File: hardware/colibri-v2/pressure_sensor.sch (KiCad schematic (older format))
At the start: 6 parts

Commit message: Annotated Components
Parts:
- gave numbers to parts that had none: 6
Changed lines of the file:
@@
 $EndDescr
 $Comp
-L BMP180 U?
+L BMP180 U6
 U 1 1 558FDE4B
 P 5950 3650
-F 0 "U?" H 6300 3950 60  0000 C CNN
+F 0 "U6" H 6300 3950 60  0000 C CNN
 F 1 "BMP180" H 5700 3350 60  0000 C CNN
 F 2 "" H 5950 3650 60  0000 C CNN
@@
 PS_I2C_SCL
 $Comp
-L R R?
+L R R44
 U 1 1 558FDE8E
 P 4600 3500
-F 0 "R?" V 4550 3650 50  0000 C CNN
+F 0 "R44" V 4550 3650 50  0000 C CNN
 F 1 "22" V 4600 3500 50  0000 C CNN
 F 2 "" V 4530 3500 30  0000 C CNN
@@
 $EndComp
 $Comp
-L R R?
+L R R45
 U 1 1 558FDECD
 P 4600 3600
-F 0 "R?" V 4550 3750 50  0000 C CNN
+F 0 "R45" V 4550 3750 50  0000 C CNN
 F 1 "22" V 4600 3600 50  0000 C CNN
 F 2 "" V 4530 3600 30  0000 C CNN
@@
 	4750 3600 5250 3600
 $Comp
-L +3V3 #PWR?
+L +3V3 #PWR57
 U 1 1 558FDF78
 P 3350 2800
-F 0 "#PWR?" H 3350 2650 50  0001 C CNN
+F 0 "#PWR57" H 3350 2650 50  0001 C CNN
 F 1 "+3V3" H 3350 2940 50  0000 C CNN
 F 2 "" H 3350 2800 60  0000 C CNN
@@
 $EndComp
 $Comp
-L +3V3 #PWR?
+L +3V3 #PWR58
 U 1 1 558FDF8F
 P 3650 2800
-F 0 "#PWR?" H 3650 2650 50  0001 C CNN
+F 0 "#PWR58" H 3650 2650 50  0001 C CNN
 F 1 "+3V3" H 3650 2940 50  0000 C CNN
 F 2 "" H 3650 2800 60  0000 C CNN
@@
 $EndComp
 $Comp
-L R R?
+L R R42
 U 1 1 558FDFA7
 P 3350 3100
-F 0 "R?" H 3250 2950 50  0000 C CNN
+F 0 "R42" H 3250 2950 50  0000 C CNN
 F 1 "2k2" V 3350 3100 50  0000 C CNN
 F 2 "" V 3280 3100 30  0000 C CNN
@@
 $EndComp
 $Comp
-L R R?
+L R R43
 U 1 1 558FE0AC
 P 3650 3100
-F 0 "R?" H 3550 2950 50  0000 C CNN
+F 0 "R43" H 3550 2950 50  0000 C CNN
 F 1 "2k2" V 3650 3100 50  0000 C CNN
 F 2 "" V 3580 3100 30  0000 C CNN
@@
 Connection ~ 7100 3500
 $Comp
-L GND #PWR?
+L GND #PWR60
 U 1 1 558FE2F6
 P 7100 4550
-F 0 "#PWR?" H 7100 4300 50  0001 C CNN
+F 0 "#PWR60" H 7100 4300 50  0001 C CNN
 F 1 "GND" H 7100 4400 50  0000 C CNN
 F 2 "" H 7100 4550 60  0000 C CNN
@@
 $EndComp
 $Comp
-L GND #PWR?
+L GND #PWR59
 U 1 1 558FE312
 P 6800 4550
-F 0 "#PWR?" H 6800 4300 50  0001 C CNN
+F 0 "#PWR59" H 6800 4300 50  0001 C CNN
 F 1 "GND" H 6800 4400 50  0000 C CNN
 F 2 "" H 6800 4550 60  0000 C CNN
@@
 	6800 3800 6800 4550
 $Comp
-L C C?
+L C C54
 U 1 1 558FE33E
 P 7100 4100
-F 0 "C?" H 7125 4200 50  0000 L CNN
+F 0 "C54" H 7125 4200 50  0000 L CNN
 F 1 "100nF" H 7125 4000 50  0000 L CNN
 F 2 "" H 7138 3950 30  0000 C CNN
@@
 	7100 2200 7100 3950
 $Comp
-L PWR_FLAG #FLG?
+L PWR_FLAG #FLG2
 U 1 1 55FF4C0A
 P 3500 1850
-F 0 "#FLG?" H 3500 1945 50  0001 C CNN
+F 0 "#FLG2" H 3500 1945 50  0001 C CNN
 F 1 "PWR_FLAG" H 3500 2030 50  0000 C CNN
 F 2 "" H 3500 1850 60  0000 C CNN

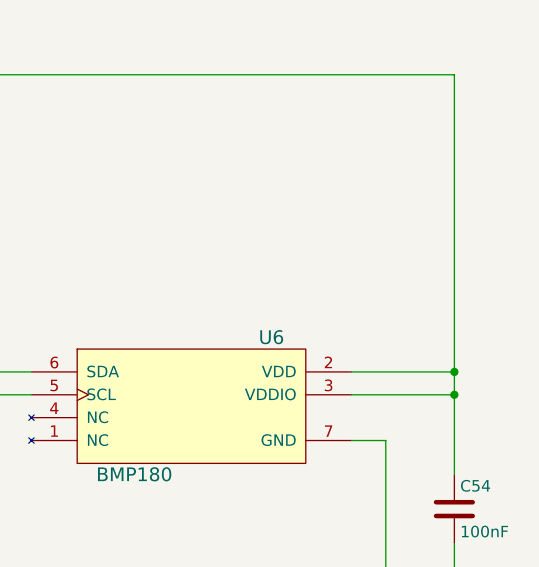
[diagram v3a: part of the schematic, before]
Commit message: Use separate VDD IO
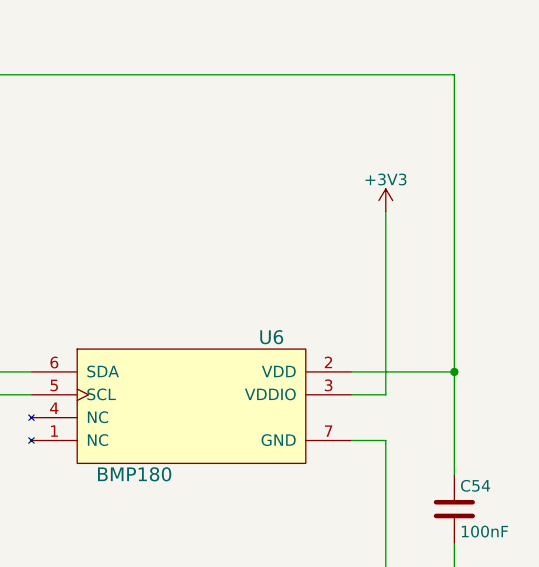
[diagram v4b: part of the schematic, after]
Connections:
- net +3V3: now also U6.3 (VDDIO)
- net V_SENS1: no longer U6.3 (VDDIO)
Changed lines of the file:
@@
 	4750 3600 5250 3600
 $Comp
-L +3V3 #PWR57
+L +3V3 #PWR058
 U 1 1 558FDF78
 P 3350 2800
-F 0 "#PWR57" H 3350 2650 50  0001 C CNN
+F 0 "#PWR058" H 3350 2650 50  0001 C CNN
 F 1 "+3V3" H 3350 2940 50  0000 C CNN
 F 2 "" H 3350 2800 60  0000 C CNN
@@
 $EndComp
 $Comp
-L +3V3 #PWR58
+L +3V3 #PWR059
 U 1 1 558FDF8F
 P 3650 2800
-F 0 "#PWR58" H 3650 2650 50  0001 C CNN
+F 0 "#PWR059" H 3650 2650 50  0001 C CNN
 F 1 "+3V3" H 3650 2940 50  0000 C CNN
 F 2 "" H 3650 2800 60  0000 C CNN
@@
 Wire Wire Line
 	7100 3500 6650 3500
-Wire Wire Line
-	7100 3600 6650 3600
 Connection ~ 7100 3500
 $Comp
-L GND #PWR60
+L GND #PWR060
 U 1 1 558FE2F6
 P 7100 4550
-F 0 "#PWR60" H 7100 4300 50  0001 C CNN
+F 0 "#PWR060" H 7100 4300 50  0001 C CNN
 F 1 "GND" H 7100 4400 50  0000 C CNN
 F 2 "" H 7100 4550 60  0000 C CNN
@@
 $EndComp
 $Comp
-L GND #PWR59
+L GND #PWR061
 U 1 1 558FE312
 P 6800 4550
-F 0 "#PWR59" H 6800 4300 50  0001 C CNN
+F 0 "#PWR061" H 6800 4300 50  0001 C CNN
 F 1 "GND" H 6800 4400 50  0000 C CNN
 F 2 "" H 6800 4550 60  0000 C CNN
@@
 	1    0    0    -1
 $EndComp
-Connection ~ 7100 3600
 Wire Wire Line
 	7100 4250 7100 4550
@@
 	7100 2200 7100 3950
 $Comp
-L PWR_FLAG #FLG2
+L PWR_FLAG #FLG062
 U 1 1 55FF4C0A
 P 3500 1850
-F 0 "#FLG2" H 3500 1945 50  0001 C CNN
+F 0 "#FLG062" H 3500 1945 50  0001 C CNN
 F 1 "PWR_FLAG" H 3500 2030 50  0000 C CNN
 F 2 "" H 3500 1850 60  0000 C CNN
@@
 	3500 1850 3500 2200
 Connection ~ 3500 2200
+$Comp
+L +3V3 #PWR?
+U 1 1 562303A9
+P 6800 2800
+F 0 "#PWR?" H 6800 2650 50  0001 C CNN
+F 1 "+3V3" H 6800 2940 50  0000 C CNN
+F 2 "" H 6800 2800 60  0000 C CNN
+F 3 "" H 6800 2800 60  0000 C CNN
+	1    6800 2800
+	1    0    0    -1
+$EndComp
+Wire Wire Line
+	6650 3600 6800 3600
+Wire Wire Line
+	6800 3600 6800 2800
 $EndSCHEMATC

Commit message: Re-annotated schematic
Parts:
- renumbered C54 to C52, R42 to R43, R43 to R44, R44 to R45, R45 to R46
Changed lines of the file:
@@
 PS_I2C_SCL
 $Comp
-L R R44
+L R R45
 U 1 1 558FDE8E
 P 4600 3500
-F 0 "R44" V 4550 3650 50  0000 C CNN
+F 0 "R45" V 4550 3650 50  0000 C CNN
 F 1 "22" V 4600 3500 50  0000 C CNN
 F 2 "" V 4530 3500 30  0000 C CNN
@@
 $EndComp
 $Comp
-L R R45
+L R R46
 U 1 1 558FDECD
 P 4600 3600
-F 0 "R45" V 4550 3750 50  0000 C CNN
+F 0 "R46" V 4550 3750 50  0000 C CNN
 F 1 "22" V 4600 3600 50  0000 C CNN
 F 2 "" V 4530 3600 30  0000 C CNN
@@
 	4750 3600 5250 3600
 $Comp
-L +3V3 #PWR058
+L +3V3 #PWR53
 U 1 1 558FDF78
 P 3350 2800
-F 0 "#PWR058" H 3350 2650 50  0001 C CNN
+F 0 "#PWR53" H 3350 2650 50  0001 C CNN
 F 1 "+3V3" H 3350 2940 50  0000 C CNN
 F 2 "" H 3350 2800 60  0000 C CNN
@@
 $EndComp
 $Comp
-L +3V3 #PWR059
+L +3V3 #PWR54
 U 1 1 558FDF8F
 P 3650 2800
-F 0 "#PWR059" H 3650 2650 50  0001 C CNN
+F 0 "#PWR54" H 3650 2650 50  0001 C CNN
 F 1 "+3V3" H 3650 2940 50  0000 C CNN
 F 2 "" H 3650 2800 60  0000 C CNN
@@
 $EndComp
 $Comp
-L R R42
+L R R43
 U 1 1 558FDFA7
 P 3350 3100
-F 0 "R42" H 3250 2950 50  0000 C CNN
+F 0 "R43" H 3250 2950 50  0000 C CNN
 F 1 "2k2" V 3350 3100 50  0000 C CNN
 F 2 "" V 3280 3100 30  0000 C CNN
@@
 $EndComp
 $Comp
-L R R43
+L R R44
 U 1 1 558FE0AC
 P 3650 3100
-F 0 "R43" H 3550 2950 50  0000 C CNN
+F 0 "R44" H 3550 2950 50  0000 C CNN
 F 1 "2k2" V 3650 3100 50  0000 C CNN
 F 2 "" V 3580 3100 30  0000 C CNN
@@
 Connection ~ 7100 3500
 $Comp
-L GND #PWR060
+L GND #PWR57
 U 1 1 558FE2F6
 P 7100 4550
-F 0 "#PWR060" H 7100 4300 50  0001 C CNN
+F 0 "#PWR57" H 7100 4300 50  0001 C CNN
 F 1 "GND" H 7100 4400 50  0000 C CNN
 F 2 "" H 7100 4550 60  0000 C CNN
@@
 $EndComp
 $Comp
-L GND #PWR061
+L GND #PWR56
 U 1 1 558FE312
 P 6800 4550
-F 0 "#PWR061" H 6800 4300 50  0001 C CNN
+F 0 "#PWR56" H 6800 4300 50  0001 C CNN
 F 1 "GND" H 6800 4400 50  0000 C CNN
 F 2 "" H 6800 4550 60  0000 C CNN
@@
 	6800 3800 6800 4550
 $Comp
-L C C54
+L C C52
 U 1 1 558FE33E
 P 7100 4100
-F 0 "C54" H 7125 4200 50  0000 L CNN
+F 0 "C52" H 7125 4200 50  0000 L CNN
 F 1 "100nF" H 7125 4000 50  0000 L CNN
 F 2 "" H 7138 3950 30  0000 C CNN
@@
 	7100 2200 7100 3950
 $Comp
-L PWR_FLAG #FLG062
+L PWR_FLAG #FLG2
 U 1 1 55FF4C0A
 P 3500 1850
-F 0 "#FLG062" H 3500 1945 50  0001 C CNN
+F 0 "#FLG2" H 3500 1945 50  0001 C CNN
 F 1 "PWR_FLAG" H 3500 2030 50  0000 C CNN
 F 2 "" H 3500 1850 60  0000 C CNN
@@
 Connection ~ 3500 2200
 $Comp
-L +3V3 #PWR?
+L +3V3 #PWR55
 U 1 1 562303A9
 P 6800 2800
-F 0 "#PWR?" H 6800 2650 50  0001 C CNN
+F 0 "#PWR55" H 6800 2650 50  0001 C CNN
 F 1 "+3V3" H 6800 2940 50  0000 C CNN
 F 2 "" H 6800 2800 60  0000 C CNN

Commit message: Associated footprints for R and some of the C
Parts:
- C52: footprint (none) -> Capacitors_SMD:C_0805
- R43, R44, R45, R46: footprint (none) -> Resistors_SMD:R_0603
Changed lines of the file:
@@
 F 0 "U6" H 6300 3950 60  0000 C CNN
 F 1 "BMP180" H 5700 3350 60  0000 C CNN
-F 2 "" H 5950 3650 60  0000 C CNN
+F 2 "" H 5950 3650 60  0001 C CNN
 F 3 "" H 5950 3650 60  0000 C CNN
 	1    5950 3650
@@
 F 0 "R45" V 4550 3650 50  0000 C CNN
 F 1 "22" V 4600 3500 50  0000 C CNN
-F 2 "" V 4530 3500 30  0000 C CNN
+F 2 "Resistors_SMD:R_0603" V 4530 3500 30  0001 C CNN
 F 3 "" H 4600 3500 30  0000 C CNN
 	1    4600 3500
@@
 F 0 "R46" V 4550 3750 50  0000 C CNN
 F 1 "22" V 4600 3600 50  0000 C CNN
-F 2 "" V 4530 3600 30  0000 C CNN
+F 2 "Resistors_SMD:R_0603" V 4530 3600 30  0001 C CNN
 F 3 "" H 4600 3600 30  0000 C CNN
 	1    4600 3600
@@
 	4750 3600 5250 3600
 $Comp
-L +3V3 #PWR53
+L +3V3 #PWR054
 U 1 1 558FDF78
 P 3350 2800
-F 0 "#PWR53" H 3350 2650 50  0001 C CNN
+F 0 "#PWR054" H 3350 2650 50  0001 C CNN
 F 1 "+3V3" H 3350 2940 50  0000 C CNN
 F 2 "" H 3350 2800 60  0000 C CNN
@@
 $EndComp
 $Comp
-L +3V3 #PWR54
+L +3V3 #PWR055
 U 1 1 558FDF8F
 P 3650 2800
-F 0 "#PWR54" H 3650 2650 50  0001 C CNN
+F 0 "#PWR055" H 3650 2650 50  0001 C CNN
 F 1 "+3V3" H 3650 2940 50  0000 C CNN
 F 2 "" H 3650 2800 60  0000 C CNN
@@
 F 0 "R43" H 3250 2950 50  0000 C CNN
 F 1 "2k2" V 3350 3100 50  0000 C CNN
-F 2 "" V 3280 3100 30  0000 C CNN
+F 2 "Resistors_SMD:R_0603" V 3280 3100 30  0001 C CNN
 F 3 "" H 3350 3100 30  0000 C CNN
 	1    3350 3100
@@
 F 0 "R44" H 3550 2950 50  0000 C CNN
 F 1 "2k2" V 3650 3100 50  0000 C CNN
-F 2 "" V 3580 3100 30  0000 C CNN
+F 2 "Resistors_SMD:R_0603" V 3580 3100 30  0001 C CNN
 F 3 "" H 3650 3100 30  0000 C CNN
 	1    3650 3100
@@
 Connection ~ 7100 3500
 $Comp
-L GND #PWR57
+L GND #PWR056
 U 1 1 558FE2F6
 P 7100 4550
-F 0 "#PWR57" H 7100 4300 50  0001 C CNN
+F 0 "#PWR056" H 7100 4300 50  0001 C CNN
 F 1 "GND" H 7100 4400 50  0000 C CNN
 F 2 "" H 7100 4550 60  0000 C CNN
@@
 $EndComp
 $Comp
-L GND #PWR56
+L GND #PWR057
 U 1 1 558FE312
 P 6800 4550
-F 0 "#PWR56" H 6800 4300 50  0001 C CNN
+F 0 "#PWR057" H 6800 4300 50  0001 C CNN
 F 1 "GND" H 6800 4400 50  0000 C CNN
 F 2 "" H 6800 4550 60  0000 C CNN
@@
 F 0 "C52" H 7125 4200 50  0000 L CNN
 F 1 "100nF" H 7125 4000 50  0000 L CNN
-F 2 "" H 7138 3950 30  0000 C CNN
+F 2 "Capacitors_SMD:C_0805" H 7138 3950 30  0001 C CNN
 F 3 "" H 7100 4100 60  0000 C CNN
 	1    7100 4100
@@
 	7100 2200 7100 3950
 $Comp
-L PWR_FLAG #FLG2
+L PWR_FLAG #FLG058
 U 1 1 55FF4C0A
 P 3500 1850
-F 0 "#FLG2" H 3500 1945 50  0001 C CNN
+F 0 "#FLG058" H 3500 1945 50  0001 C CNN
 F 1 "PWR_FLAG" H 3500 2030 50  0000 C CNN
 F 2 "" H 3500 1850 60  0000 C CNN
@@
 Connection ~ 3500 2200
 $Comp
-L +3V3 #PWR55
+L +3V3 #PWR059
 U 1 1 562303A9
 P 6800 2800
-F 0 "#PWR55" H 6800 2650 50  0001 C CNN
+F 0 "#PWR059" H 6800 2650 50  0001 C CNN
 F 1 "+3V3" H 6800 2940 50  0000 C CNN
 F 2 "" H 6800 2800 60  0000 C CNN

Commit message: Work on cortex USB connection.
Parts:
- removed C52: 100nF, Capacitors_SMD:C_0805, symbol C
- removed R43, R44: 2k2, Resistors_SMD:R_0603, symbol R
- removed R45, R46: 22, Resistors_SMD:R_0603, symbol R
- added C?: 100nF/50V, Capacitors_SMD:C_0603, symbol C_SMT
- added R? (x2): 2k2/5%, Resistors_SMD:R_0603, symbol R_SMT
- added R? (x2): 22R/5%, Resistors_SMD:R_0603, symbol R_SMT
- renumbered U6 to U?
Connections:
- net +3V3: now also R?.1, R?.1
- net GND: now also C?.2
- net PS_I2C_SCL: now also R?.2, R?.2
- net PS_I2C_SDA: now also R?.2, R?.2
- net V_SENS1: now also C?.1
- net at U?.5 (SCL): now also R?.1
- net at U?.6 (SDA): now also R?.1
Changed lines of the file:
@@
 $EndDescr
 $Comp
-L BMP180 U6
+L BMP180 U?
 U 1 1 558FDE4B
 P 5950 3650
-F 0 "U6" H 6300 3950 60  0000 C CNN
+F 0 "U?" H 6300 3950 60  0000 C CNN
 F 1 "BMP180" H 5700 3350 60  0000 C CNN
 F 2 "" H 5950 3650 60  0001 C CNN
@@
 Text HLabel 2950 3600 0    60   Input ~ 0
 PS_I2C_SCL
-$Comp
-L R R45
-U 1 1 558FDE8E
-P 4600 3500
-F 0 "R45" V 4550 3650 50  0000 C CNN
-F 1 "22" V 4600 3500 50  0000 C CNN
-F 2 "Resistors_SMD:R_0603" V 4530 3500 30  0001 C CNN
-F 3 "" H 4600 3500 30  0000 C CNN
-	1    4600 3500
-	0    1    1    0
-$EndComp
-$Comp
-L R R46
-U 1 1 558FDECD
-P 4600 3600
-F 0 "R46" V 4550 3750 50  0000 C CNN
-F 1 "22" V 4600 3600 50  0000 C CNN
-F 2 "Resistors_SMD:R_0603" V 4530 3600 30  0001 C CNN
-F 3 "" H 4600 3600 30  0000 C CNN
-	1    4600 3600
-	0    1    1    0
-$EndComp
 Wire Wire Line
 	2950 3500 4450 3500
@@
 	4750 3600 5250 3600
 $Comp
-L +3V3 #PWR054
+L +3V3 #PWR?
 U 1 1 558FDF78
 P 3350 2800
-F 0 "#PWR054" H 3350 2650 50  0001 C CNN
+F 0 "#PWR?" H 3350 2650 50  0001 C CNN
 F 1 "+3V3" H 3350 2940 50  0000 C CNN
 F 2 "" H 3350 2800 60  0000 C CNN
@@
 $EndComp
 $Comp
-L +3V3 #PWR055
+L +3V3 #PWR?
 U 1 1 558FDF8F
 P 3650 2800
-F 0 "#PWR055" H 3650 2650 50  0001 C CNN
+F 0 "#PWR?" H 3650 2650 50  0001 C CNN
 F 1 "+3V3" H 3650 2940 50  0000 C CNN
 F 2 "" H 3650 2800 60  0000 C CNN
@@
 	1    3650 2800
 	1    0    0    -1
-$EndComp
-$Comp
-L R R43
-U 1 1 558FDFA7
-P 3350 3100
-F 0 "R43" H 3250 2950 50  0000 C CNN
-F 1 "2k2" V 3350 3100 50  0000 C CNN
-F 2 "Resistors_SMD:R_0603" V 3280 3100 30  0001 C CNN
-F 3 "" H 3350 3100 30  0000 C CNN
-	1    3350 3100
-	-1   0    0    1
-$EndComp
-$Comp
-L R R44
-U 1 1 558FE0AC
-P 3650 3100
-F 0 "R44" H 3550 2950 50  0000 C CNN
-F 1 "2k2" V 3650 3100 50  0000 C CNN
-F 2 "Resistors_SMD:R_0603" V 3580 3100 30  0001 C CNN
-F 3 "" H 3650 3100 30  0000 C CNN
-	1    3650 3100
-	-1   0    0    1
 $EndComp
 Wire Wire Line
@@
 Connection ~ 7100 3500
 $Comp
-L GND #PWR056
+L GND #PWR?
 U 1 1 558FE2F6
 P 7100 4550
-F 0 "#PWR056" H 7100 4300 50  0001 C CNN
+F 0 "#PWR?" H 7100 4300 50  0001 C CNN
 F 1 "GND" H 7100 4400 50  0000 C CNN
 F 2 "" H 7100 4550 60  0000 C CNN
@@
 $EndComp
 $Comp
-L GND #PWR057
+L GND #PWR?
 U 1 1 558FE312
 P 6800 4550
-F 0 "#PWR057" H 6800 4300 50  0001 C CNN
+F 0 "#PWR?" H 6800 4300 50  0001 C CNN
 F 1 "GND" H 6800 4400 50  0000 C CNN
 F 2 "" H 6800 4550 60  0000 C CNN
@@
 Wire Wire Line
 	6800 3800 6800 4550
-$Comp
-L C C52
-U 1 1 558FE33E
-P 7100 4100
-F 0 "C52" H 7125 4200 50  0000 L CNN
-F 1 "100nF" H 7125 4000 50  0000 L CNN
-F 2 "Capacitors_SMD:C_0805" H 7138 3950 30  0001 C CNN
-F 3 "" H 7100 4100 60  0000 C CNN
-	1    7100 4100
-	1    0    0    -1
-$EndComp
 Wire Wire Line
 	7100 4250 7100 4550
@@
 	7100 2200 7100 3950
 $Comp
-L PWR_FLAG #FLG058
+L PWR_FLAG #FLG?
 U 1 1 55FF4C0A
 P 3500 1850
-F 0 "#FLG058" H 3500 1945 50  0001 C CNN
+F 0 "#FLG?" H 3500 1945 50  0001 C CNN
 F 1 "PWR_FLAG" H 3500 2030 50  0000 C CNN
 F 2 "" H 3500 1850 60  0000 C CNN
@@
 Connection ~ 3500 2200
 $Comp
-L +3V3 #PWR059
+L +3V3 #PWR?
 U 1 1 562303A9
 P 6800 2800
-F 0 "#PWR059" H 6800 2650 50  0001 C CNN
+F 0 "#PWR?" H 6800 2650 50  0001 C CNN
 F 1 "+3V3" H 6800 2940 50  0000 C CNN
 F 2 "" H 6800 2800 60  0000 C CNN
@@
 Wire Wire Line
 	6800 3600 6800 2800
+$Comp
+L R_SMT R?
+U 1 1 562F15F5
+P 3650 3100
+F 0 "R?" V 3720 3100 50  0000 C CNN
+F 1 "2k2/5%" V 3580 3100 50  0000 C CNN
+F 2 "Resistors_SMD:R_0603" V 3800 3100 30  0001 C CNN
+F 3 "" V 3730 3100 30  0000 C CNN
+F 4 "0603" V 3650 3100 20  0000 C CNN "SMT"
+F 5 "9331913" V 3850 3100 30  0001 C CNN "Part"
+F 6 "Farnell" V 3900 3100 30  0001 C CNN "Provider"
+	1    3650 3100
+	1    0    0    -1
+$EndComp
+$Comp
+L R_SMT R?
+U 1 1 562F1678
+P 3350 3100
+F 0 "R?" V 3420 3100 50  0000 C CNN
+F 1 "2k2/5%" V 3280 3100 50  0000 C CNN
+F 2 "Resistors_SMD:R_0603" V 3500 3100 30  0001 C CNN
+F 3 "" V 3430 3100 30  0000 C CNN
+F 4 "0603" V 3350 3100 20  0000 C CNN "SMT"
+F 5 "9331913" V 3550 3100 30  0001 C CNN "Part"
+F 6 "Farnell" V 3600 3100 30  0001 C CNN "Provider"
+	1    3350 3100
+	1    0    0    -1
+$EndComp
+$Comp
+L R_SMT R?
+U 1 1 562F16F0
+P 4600 3500
+F 0 "R?" V 4550 3700 50  0000 C CNN
+F 1 "22R/5%" V 4550 3250 50  0000 C CNN
+F 2 "Resistors_SMD:R_0603" V 4750 3500 30  0001 C CNN
+F 3 "" V 4680 3500 30  0000 C CNN
+F 4 "0603" V 4600 3500 20  0000 C CNN "SMT"
+F 5 "9331891" V 4800 3500 30  0001 C CNN "Part"
+F 6 "Farnell" V 4850 3500 30  0001 C CNN "Provider"
+	1    4600 3500
+	0    1    1    0
+$EndComp
+$Comp
+L R_SMT R?
+U 1 1 562F17F9
+P 4600 3600
+F 0 "R?" V 4650 3800 50  0000 C CNN
+F 1 "22R/5%" V 4650 3350 50  0000 C CNN
+F 2 "Resistors_SMD:R_0603" V 4750 3600 30  0001 C CNN
+F 3 "" V 4680 3600 30  0000 C CNN
+F 4 "0603" V 4600 3600 20  0000 C CNN "SMT"
+F 5 "9331891" V 4800 3600 30  0001 C CNN "Part"
+F 6 "Farnell" V 4850 3600 30  0001 C CNN "Provider"
+	1    4600 3600
+	0    1    1    0
+$EndComp
+$Comp
+L C_SMT C?
+U 1 1 562F2485
+P 7100 4100
+F 0 "C?" H 7125 4200 50  0000 L CNN
+F 1 "100nF/50V" H 7125 4000 50  0000 L CNN
+F 2 "Capacitors_SMD:C_0603" H 7130 3950 30  0001 L CNN
+F 3 "" H 7125 4200 60  0000 L CNN
+F 4 "0603" H 7100 4100 20  0000 C CNN "SMT"
+F 5 "1414028" H 7130 3910 30  0001 L CNN "Part"
+F 6 "Farnell" H 7130 3870 30  0001 L CNN "Provider"
+	1    7100 4100
+	1    0    0    -1
+$EndComp
 $EndSCHEMATC
